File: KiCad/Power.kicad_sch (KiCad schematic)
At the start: 23 parts, among them U24 173010578, U25 AP1117-33, U26 AP1117-33

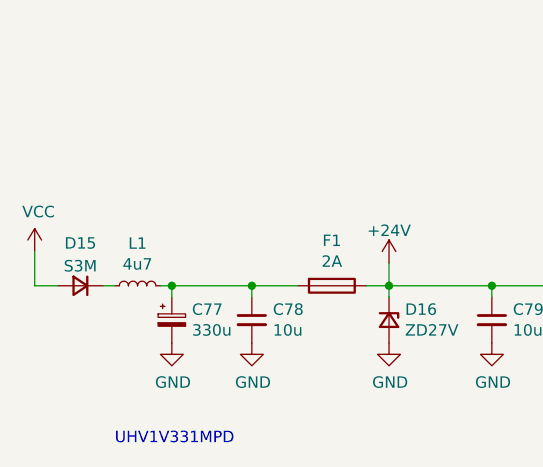
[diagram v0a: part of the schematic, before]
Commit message: Port to Kicad 7, small changes in auto-reset feature
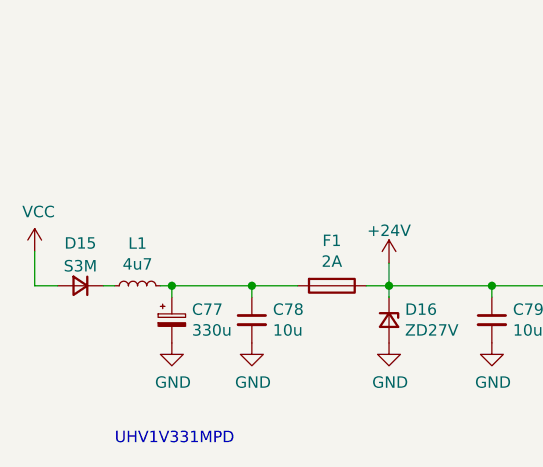
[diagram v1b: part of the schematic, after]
